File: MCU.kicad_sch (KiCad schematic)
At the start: 31 parts, among them J5 Micro_SD_Card, U4 EFM32GG332, Y1 Crystal_GND23

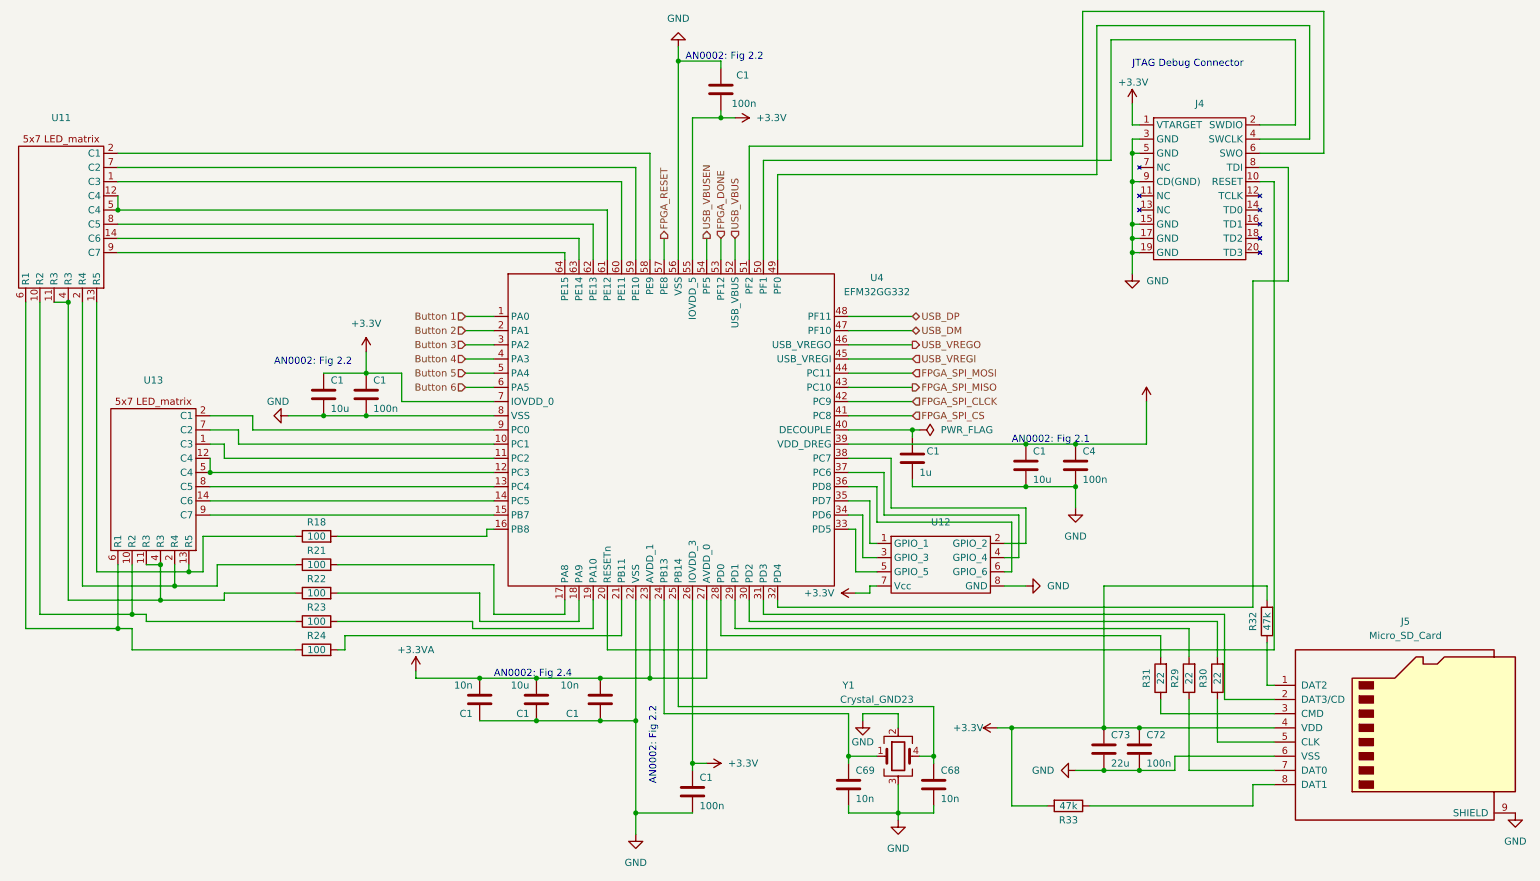
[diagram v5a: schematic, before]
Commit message: Added footprints to symbols
Some nice light work
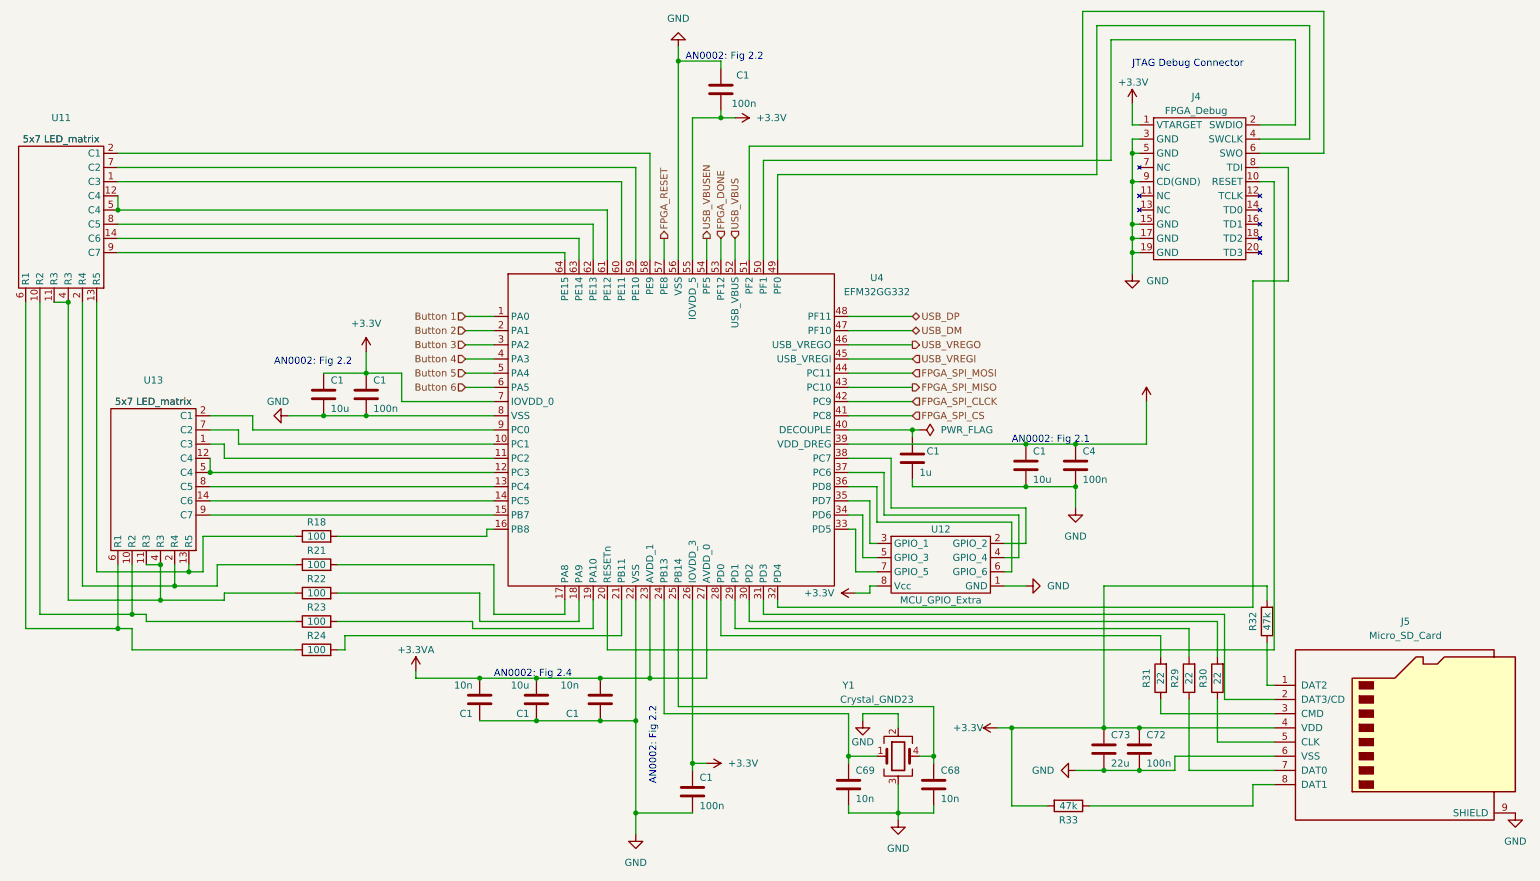
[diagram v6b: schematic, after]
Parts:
- C1, C4, C68, C69, C72, C73: footprint (none) -> Capacitor_SMD:C_1206_3216Metric
- J4: value ~ -> FPGA_Debug; footprint (none) -> Connector_PinHeader_2.54mm:PinHeader_2x10_P2.54mm_Vertical
- J5: footprint (none) -> Connector_Card:microSD_HC_Hirose_DM3BT-DSF-PEJS
- R18, R21, R22, R23, R24, R29, R30, R31, R32, R33: footprint (none) -> Resistor_SMD:R_1206_3216Metric
- U11, U13: value ~ -> 5x7 LED_matrix; footprint (none) -> LED_TA20-11SRWA:LED_TA20-11SRWA
- U12: value ~ -> MCU_GPIO_Extra; footprint (none) -> Connector_PinHeader_2.54mm:PinHeader_2x04_P2.54mm_Vertical
- U4: footprint (none) -> Package_QFP:TQFP-64_10x10mm_P0.5mm
- Y1: footprint (none) -> Crystal:Crystal_SMD_Abracon_ABM8G-4Pin_3.2x2.5mm
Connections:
- net +3.3V: now also U12.8 (Vcc); no longer U12.7 (Vcc)
- net GND: now also U12.1 (GND); no longer U12.8 (GND)
- net at U4.35 (PD7): now also U12.3 (GPIO_1); no longer U12.1 (GPIO_1)
- net at U4.34 (PD6): now also U12.5 (GPIO_3); no longer U12.3 (GPIO_3)
- net at U4.33 (PD5): now also U12.7 (GPIO_5); no longer U12.5 (GPIO_5)
- new net: R21.1, U11.2 (R4), U13.2 (R4)

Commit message: Started implementing physical layout
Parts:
- removed J5: Micro_SD_Card, Connector_Card:microSD_HC_Hirose_DM3BT-DSF-PEJS, symbol Connector:Micro_SD_Card
- added J6: Micro_SD_Card_Det_Hirose_DM3AT, Connector_Card:microSD_HC_Hirose_DM3BT-DSF-PEJS, symbol Connector:Micro_SD_Card_Det_Hirose_DM3AT
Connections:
- net +3.3V: now also J6.4 (VDD)
- net GND: now also J6.10 (DET_A), J6.11 (SHIELD), J6.6 (VSS), J6.9 (DET_B)
- net at R29.1: now also J6.7 (DAT0)
- net at U4.31 (PD3): now also J6.2 (DAT3/CD)
- net at R32.1: now also J6.1 (DAT2)
- net at R31.1: now also J6.3 (CMD)
- net at R30.1: now also J6.5 (CLK)
- net at R33.1: now also J6.8 (DAT1)
- new net: R21.1, U11.3 (R4), U13.3 (R4)

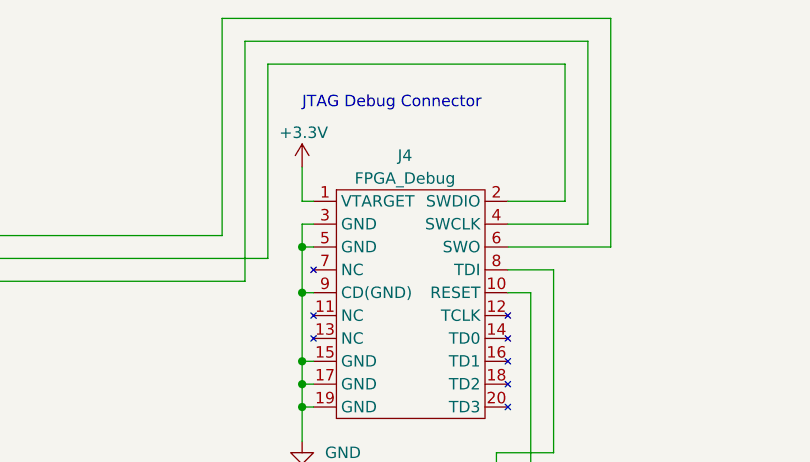
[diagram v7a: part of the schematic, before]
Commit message: First pass at placing components physically
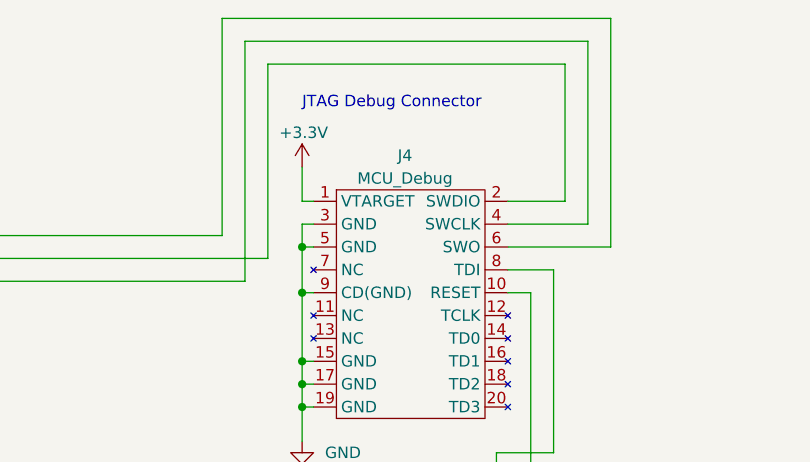
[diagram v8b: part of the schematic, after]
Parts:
- J4: value FPGA_Debug -> MCU_Debug
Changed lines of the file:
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@@
       (effects (font (size 1.27 1.27)))
     )
-    (property "Value" "FPGA_Debug" (at 224.79 36.83 0)
+    (property "Value" "MCU_Debug" (at 224.79 36.83 0)
       (effects (font (size 1.27 1.27)))
     )
